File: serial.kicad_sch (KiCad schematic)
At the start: 61 parts, among them J201 Debug, J202 RS-232, J203 RS-485/422, U201 ADM213, U202 SP330

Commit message: Revisit 3D models
Signed-off-by: Benedikt Spranger <b.spranger@linutronix.de>
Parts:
- D201, D202, D203, D204, D205, D206, D207, D208, D209, D210, D211, D212, D213, D214: footprint LED_SMD:LED_Kingbright_AAA3528ESGCT -> fixes:LED_Kingbright_AAA3528ESGCT
- J203: footprint TerminalBlock_WAGO:TerminalBlock_WAGO_236-404_1x04_P5.00mm_45Degree -> fixes:TerminalBlock_WAGO_236-404_1x04_P5.00mm_45Degree
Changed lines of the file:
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@@
 			)
 		)
-		(property "Footprint" "LED_SMD:LED_Kingbright_AAA3528ESGCT"
+		(property "Footprint" "fixes:LED_Kingbright_AAA3528ESGCT"
 			(at 241.3 148.082 0)
 			(effects
@@
 			)
 		)
-		(property "Footprint" "LED_SMD:LED_Kingbright_AAA3528ESGCT"
+		(property "Footprint" "fixes:LED_Kingbright_AAA3528ESGCT"
 			(at 215.9 148.082 0)
 			(effects
@@
 			)
 		)
-		(property "Footprint" "LED_SMD:LED_Kingbright_AAA3528ESGCT"
+		(property "Footprint" "fixes:LED_Kingbright_AAA3528ESGCT"
 			(at 215.9 97.282 0)
 			(effects
@@
 			)
 		)
-		(property "Footprint" "LED_SMD:LED_Kingbright_AAA3528ESGCT"
+		(property "Footprint" "fixes:LED_Kingbright_AAA3528ESGCT"
 			(at 62.23 46.482 0)
 			(effects
@@
 			)
 		)
-		(property "Footprint" "LED_SMD:LED_Kingbright_AAA3528ESGCT"
+		(property "Footprint" "fixes:LED_Kingbright_AAA3528ESGCT"
 			(at 114.3 46.482 0)
 			(effects
@@
 			)
 		)
-		(property "Footprint" "LED_SMD:LED_Kingbright_AAA3528ESGCT"
+		(property "Footprint" "fixes:LED_Kingbright_AAA3528ESGCT"
 			(at 241.3 97.282 0)
 			(effects
@@
 			)
 		)
-		(property "Footprint" "LED_SMD:LED_Kingbright_AAA3528ESGCT"
+		(property "Footprint" "fixes:LED_Kingbright_AAA3528ESGCT"
 			(at 215.9 46.482 0)
 			(effects
@@
 			)
 		)
-		(property "Footprint" "LED_SMD:LED_Kingbright_AAA3528ESGCT"
+		(property "Footprint" "fixes:LED_Kingbright_AAA3528ESGCT"
 			(at 139.7 46.482 0)
 			(effects
@@
 			)
 		)
-		(property "Footprint" "LED_SMD:LED_Kingbright_AAA3528ESGCT"
+		(property "Footprint" "fixes:LED_Kingbright_AAA3528ESGCT"
 			(at 165.1 46.482 0)
 			(effects
@@
 			)
 		)
-		(property "Footprint" "LED_SMD:LED_Kingbright_AAA3528ESGCT"
+		(property "Footprint" "fixes:LED_Kingbright_AAA3528ESGCT"
 			(at 36.83 46.482 0)
 			(effects
@@
 			)
 		)
-		(property "Footprint" "LED_SMD:LED_Kingbright_AAA3528ESGCT"
+		(property "Footprint" "fixes:LED_Kingbright_AAA3528ESGCT"
 			(at 88.9 46.482 0)
 			(effects
@@
 			)
 		)
-		(property "Footprint" "LED_SMD:LED_Kingbright_AAA3528ESGCT"
+		(property "Footprint" "fixes:LED_Kingbright_AAA3528ESGCT"
 			(at 241.3 46.482 0)
 			(effects
@@
 			)
 		)
-		(property "Footprint" "LED_SMD:LED_Kingbright_AAA3528ESGCT"
+		(property "Footprint" "fixes:LED_Kingbright_AAA3528ESGCT"
 			(at 190.5 46.482 0)
 			(effects
@@
 			)
 		)
-		(property "Footprint" "LED_SMD:LED_Kingbright_AAA3528ESGCT"
+		(property "Footprint" "fixes:LED_Kingbright_AAA3528ESGCT"
 			(at 266.7 46.482 0)
 			(effects
@@
 			)
 		)
-		(property "Footprint" "TerminalBlock_WAGO:TerminalBlock_WAGO_236-404_1x04_P5.00mm_45Degree"
+		(property "Footprint" "fixes:TerminalBlock_WAGO_236-404_1x04_P5.00mm_45Degree"
 			(at 187.96 137.16 0)
 			(effects

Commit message: Fix Dual LED footprint issue
Signed-off-by: Benedikt Spranger <b.spranger@linutronix.de>
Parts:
- D201, D202, D203, D204, D205, D206, D207, D208, D209, D210, D211, D212, D213, D214: symbol Device:LED_Dual_AAKK -> led:LED_Dual_KAAK
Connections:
- net CTS: now also D212.1 (K2); no longer D212.4 (K2)
- net GND: now also D201.4 (K1), D202.4 (K1), D203.4 (K1), D204.4 (K1), D205.4 (K1), D206.4 (K1), D207.4 (K1), D208.4 (K1), D209.4 (K1), D210.4 (K1), D211.4 (K1), D212.4 (K1), D213.4 (K1), D214.4 (K1); no longer D201.3 (K1), D202.3 (K1), D203.3 (K1), D204.3 (K1), D205.3 (K1), D206.3 (K1), D207.3 (K1), D208.3 (K1), D209.3 (K1), D210.3 (K1), D211.3 (K1), D212.3 (K1), D213.3 (K1), D214.3 (K1)
- net RTS: now also D213.1 (K2); no longer D213.4 (K2)
- net RXD: now also D210.1 (K2); no longer D210.4 (K2)
- net TXD: now also D209.1 (K2); no longer D209.4 (K2)
- net USART2_CTS: now also D205.1 (K2); no longer D205.4 (K2)
- net USART2_DCD: now also D207.1 (K2); no longer D207.4 (K2)
- net USART2_DSR: now also D208.1 (K2); no longer D208.4 (K2)
- net USART2_DTR: now also D211.1 (K2); no longer D211.4 (K2)
- net USART2_RI: now also D214.1 (K2); no longer D214.4 (K2)
- net USART2_RTS: now also D206.1 (K2); no longer D206.4 (K2)
- net USART2_RX: now also D203.1 (K2); no longer D203.4 (K2)
- net USART2_TX: now also D204.1 (K2); no longer D204.4 (K2)
- net USART3_RX: now also D201.1 (K2); no longer D201.4 (K2)
- net USART3_TX: now also D202.1 (K2); no longer D202.4 (K2)
- net at R230.2: now also D213.3 (A1); no longer D213.1 (A1)
- net at R224.2: now also D210.3 (A1); no longer D210.1 (A1)
- net at R223.2: now also D209.3 (A1); no longer D209.1 (A1)
- net at R229.2: now also D212.3 (A1); no longer D212.1 (A1)
- net at R212.2: now also D206.3 (A1); no longer D206.1 (A1)
- net at R204.2: now also D202.3 (A1); no longer D202.1 (A1)
- net at R208.2: now also D204.3 (A1); no longer D204.1 (A1)
- net at R222.2: now also D208.3 (A1); no longer D208.1 (A1)
- net at R210.2: now also D205.3 (A1); no longer D205.1 (A1)
- net at R202.2: now also D201.3 (A1); no longer D201.1 (A1)
- net at R206.2: now also D203.3 (A1); no longer D203.1 (A1)
- net at R218.2: now also D207.3 (A1); no longer D207.1 (A1)
- net at R228.2: now also D211.3 (A1); no longer D211.1 (A1)
- net at R232.2: now also D214.3 (A1); no longer D214.1 (A1)
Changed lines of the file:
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@@
 	)
 	(symbol
-		(lib_id "Device:LED_Dual_AAKK")
+		(lib_id "led:LED_Dual_KAAK")
 		(at 241.3 147.32 270)
 		(unit 1)
@@
 			)
 		)
-		(property "Description" "Dual LED, cathodes on pins 3 and 4"
+		(property "Description" "Dual LED, cathodes on pins 1 and 4"
 			(at 241.3 147.32 0)
 			(effects
@@
 	)
 	(symbol
-		(lib_id "Device:LED_Dual_AAKK")
+		(lib_id "led:LED_Dual_KAAK")
 		(at 215.9 147.32 270)
 		(unit 1)
@@
 			)
 		)
-		(property "Description" "Dual LED, cathodes on pins 3 and 4"
+		(property "Description" "Dual LED, cathodes on pins 1 and 4"
 			(at 215.9 147.32 0)
 			(effects
@@
 	)
 	(symbol
-		(lib_id "Device:LED_Dual_AAKK")
+		(lib_id "led:LED_Dual_KAAK")
 		(at 215.9 96.52 270)
 		(unit 1)
@@
 			)
 		)
-		(property "Description" "Dual LED, cathodes on pins 3 and 4"
+		(property "Description" "Dual LED, cathodes on pins 1 and 4"
 			(at 215.9 96.52 0)
 			(effects
@@
 	)
 	(symbol
-		(lib_id "Device:LED_Dual_AAKK")
+		(lib_id "led:LED_Dual_KAAK")
 		(at 62.23 45.72 270)
 		(unit 1)
@@
 			)
 		)
-		(property "Description" "Dual LED, cathodes on pins 3 and 4"
+		(property "Description" "Dual LED, cathodes on pins 1 and 4"
 			(at 62.23 45.72 0)
 			(effects
@@
 	)
 	(symbol
-		(lib_id "Device:LED_Dual_AAKK")
+		(lib_id "led:LED_Dual_KAAK")
 		(at 114.3 45.72 270)
 		(unit 1)
@@
 			)
 		)
-		(property "Description" "Dual LED, cathodes on pins 3 and 4"
+		(property "Description" "Dual LED, cathodes on pins 1 and 4"
 			(at 114.3 45.72 0)
 			(effects
@@
 	)
 	(symbol
-		(lib_id "Device:LED_Dual_AAKK")
+		(lib_id "led:LED_Dual_KAAK")
 		(at 241.3 96.52 270)
 		(unit 1)
@@
 			)
 		)
-		(property "Description" "Dual LED, cathodes on pins 3 and 4"
+		(property "Description" "Dual LED, cathodes on pins 1 and 4"
 			(at 241.3 96.52 0)
 			(effects
@@
 	)
 	(symbol
-		(lib_id "Device:LED_Dual_AAKK")
+		(lib_id "led:LED_Dual_KAAK")
 		(at 215.9 45.72 270)
 		(unit 1)
@@
 			)
 		)
-		(property "Description" "Dual LED, cathodes on pins 3 and 4"
+		(property "Description" "Dual LED, cathodes on pins 1 and 4"
 			(at 215.9 45.72 0)
 			(effects
@@
 	)
 	(symbol
-		(lib_id "Device:LED_Dual_AAKK")
+		(lib_id "led:LED_Dual_KAAK")
 		(at 139.7 45.72 270)
 		(unit 1)
@@
 			)
 		)
-		(property "Description" "Dual LED, cathodes on pins 3 and 4"
+		(property "Description" "Dual LED, cathodes on pins 1 and 4"
 			(at 139.7 45.72 0)
 			(effects
@@
 	)
 	(symbol
-		(lib_id "Device:LED_Dual_AAKK")
+		(lib_id "led:LED_Dual_KAAK")
 		(at 165.1 45.72 270)
 		(unit 1)
@@
 			)
 		)
-		(property "Description" "Dual LED, cathodes on pins 3 and 4"
+		(property "Description" "Dual LED, cathodes on pins 1 and 4"
 			(at 165.1 45.72 0)
 			(effects
@@
 	)
 	(symbol
-		(lib_id "Device:LED_Dual_AAKK")
+		(lib_id "led:LED_Dual_KAAK")
 		(at 36.83 45.72 270)
 		(unit 1)
@@
 			)
 		)
-		(property "Description" "Dual LED, cathodes on pins 3 and 4"
+		(property "Description" "Dual LED, cathodes on pins 1 and 4"
 			(at 36.83 45.72 0)
 			(effects
@@
 			)
 		)
+		(property "digikey#" ""
+			(at 36.83 45.72 0)
+			(effects
+				(font
+					(size 1.27 1.27)
+				)
+				(hide yes)
+			)
+		)
+		(property "tme#" ""
+			(at 36.83 45.72 0)
+			(effects
+				(font
+					(size 1.27 1.27)
+				)
+				(hide yes)
+			)
+		)
 		(pin "2"
 		)
@@
 	)
 	(symbol
-		(lib_id "Device:LED_Dual_AAKK")
+		(lib_id "led:LED_Dual_KAAK")
 		(at 88.9 45.72 270)
 		(unit 1)
@@
 			)
 		)
-		(property "Description" "Dual LED, cathodes on pins 3 and 4"
+		(property "Description" "Dual LED, cathodes on pins 1 and 4"
 			(at 88.9 45.72 0)
 			(effects
@@
 	)
 	(symbol
-		(lib_id "Device:LED_Dual_AAKK")
+		(lib_id "led:LED_Dual_KAAK")
 		(at 241.3 45.72 270)
 		(unit 1)
@@
 			)
 		)
-		(property "Description" "Dual LED, cathodes on pins 3 and 4"
+		(property "Description" "Dual LED, cathodes on pins 1 and 4"
 			(at 241.3 45.72 0)
 			(effects
@@
 	)
 	(symbol
-		(lib_id "Device:LED_Dual_AAKK")
+		(lib_id "led:LED_Dual_KAAK")
 		(at 190.5 45.72 270)
 		(unit 1)
@@
 			)
 		)
-		(property "Description" "Dual LED, cathodes on pins 3 and 4"
+		(property "Description" "Dual LED, cathodes on pins 1 and 4"
 			(at 190.5 45.72 0)
 			(effects
@@
 	)
 	(symbol
-		(lib_id "Device:LED_Dual_AAKK")
+		(lib_id "led:LED_Dual_KAAK")
 		(at 266.7 45.72 270)
 		(unit 1)
@@
 			)
 		)
-		(property "Description" "Dual LED, cathodes on pins 3 and 4"
+		(property "Description" "Dual LED, cathodes on pins 1 and 4"
 			(at 266.7 45.72 0)
 			(effects

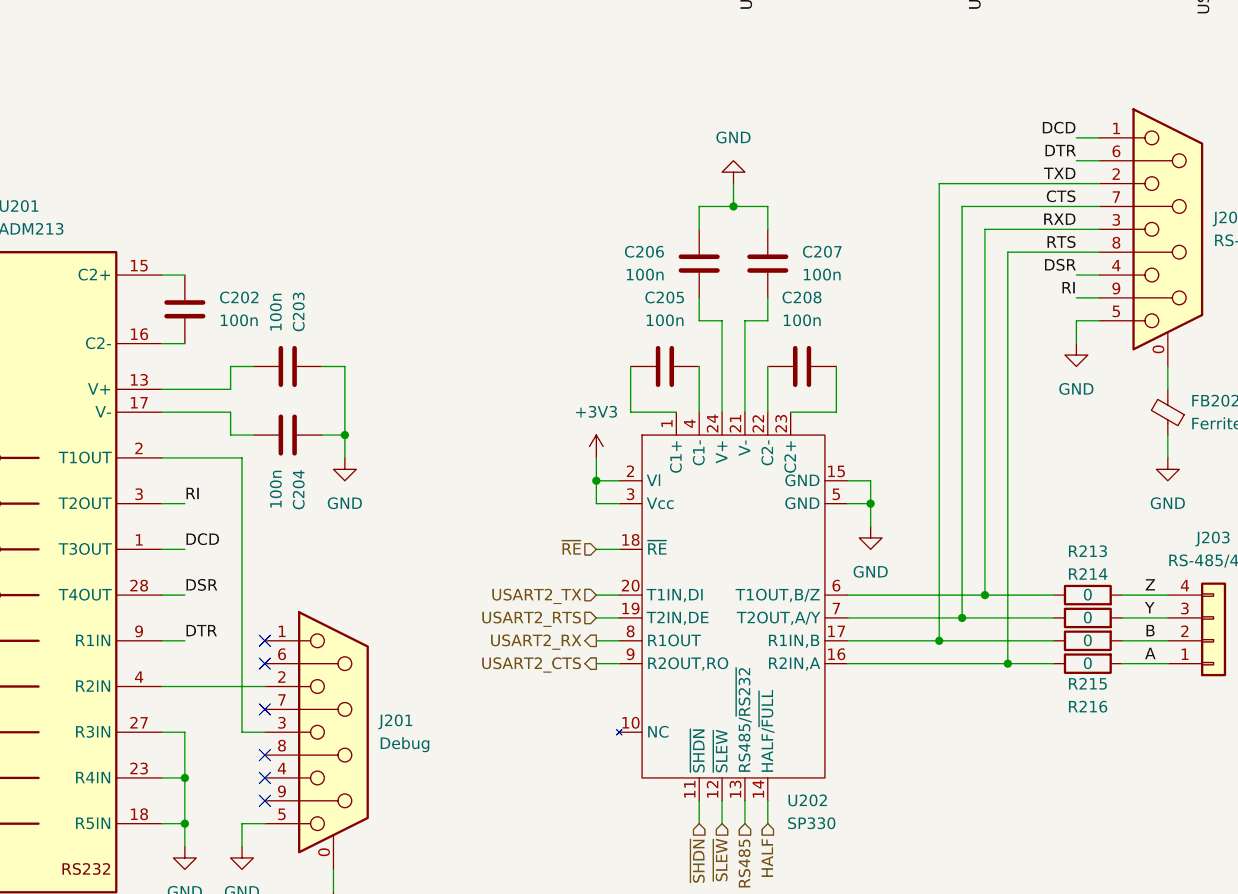
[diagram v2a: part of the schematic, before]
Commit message: Rework serial from DTE to DCE
Signed-off-by: Benedikt Spranger <b.spranger@linutronix.de>
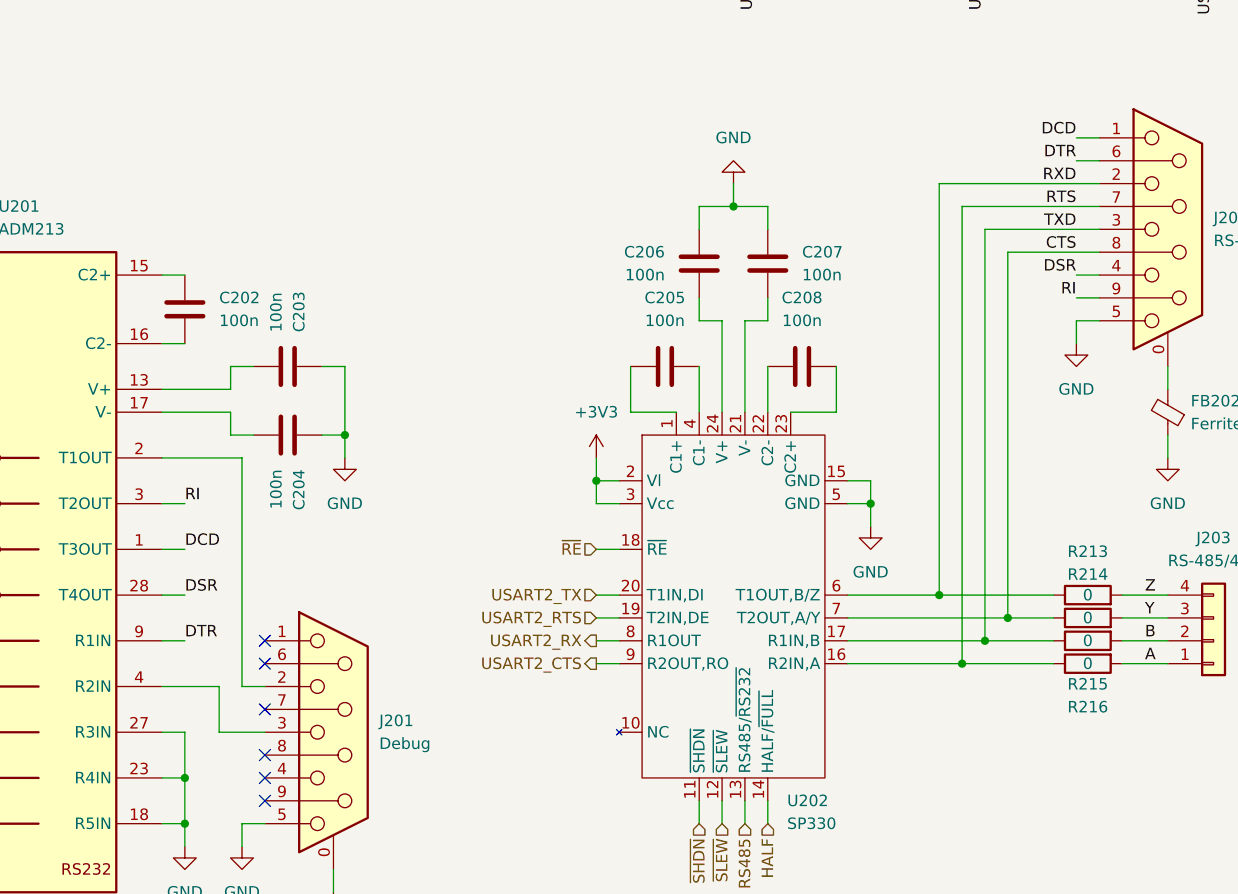
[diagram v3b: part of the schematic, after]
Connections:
- net CTS: now also J202.8; no longer J202.7
- net RTS: now also J202.7; no longer J202.8
- net RXD: now also J202.2; no longer J202.3
- net TXD: now also J202.3; no longer J202.2
- net at U201.2 (T1OUT): now also J201.2; no longer J201.3
- net at U201.4 (R2IN): now also J201.3; no longer J201.2
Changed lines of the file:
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@@
-	)
-	(junction
-		(at 165.1 139.7)
-		(diameter 0)
-		(color 0 0 0 0)
 	)
 	(junction
@@
 	)
 	(junction
+		(at 160.02 139.7)
+		(diameter 0)
+		(color 0 0 0 0)
+	)
+	(junction
+		(at 162.56 137.16)
+		(diameter 0)
+		(color 0 0 0 0)
+	)
+	(junction
+		(at 157.48 132.08)
+		(diameter 0)
+		(color 0 0 0 0)
+	)
+	(junction
 		(at 134.62 88.9)
 		(diameter 0)
@@
 	)
 	(junction
-		(at 160.02 134.62)
-		(diameter 0)
-		(color 0 0 0 0)
-	)
-	(junction
-		(at 162.56 132.08)
+		(at 165.1 134.62)
 		(diameter 0)
 		(color 0 0 0 0)
@@
 		(color 0 0 0 0)
 	)
-	(junction
-		(at 157.48 137.16)
-		(diameter 0)
-		(color 0 0 0 0)
-	)
 	(no_connect
 		(at 82.55 149.86)
@@
 	(wire
 		(pts
+			(xy 77.47 142.24) (xy 77.47 147.32)
+		)
+		(stroke
+			(width 0)
+			(type default)
+		)
+	)
+	(wire
+		(pts
 			(xy 27.94 127) (xy 30.48 127)
 		)
@@
 	(wire
 		(pts
-			(xy 165.1 93.98) (xy 165.1 139.7)
-		)
-		(stroke
-			(width 0)
-			(type default)
-		)
-	)
-	(wire
-		(pts
 			(xy 243.84 25.4) (xy 243.84 27.94)
 		)
@@
 	(wire
 		(pts
+			(xy 157.48 132.08) (xy 170.18 132.08)
+		)
+		(stroke
+			(width 0)
+			(type default)
+		)
+	)
+	(wire
+		(pts
 			(xy 243.84 53.34) (xy 243.84 55.88)
 		)
@@
 	(wire
 		(pts
-			(xy 147.32 139.7) (xy 165.1 139.7)
+			(xy 147.32 139.7) (xy 160.02 139.7)
 		)
 		(stroke
@@
 	(wire
 		(pts
-			(xy 147.32 132.08) (xy 162.56 132.08)
+			(xy 147.32 132.08) (xy 157.48 132.08)
 		)
 		(stroke
@@
 	(wire
 		(pts
-			(xy 160.02 134.62) (xy 170.18 134.62)
-		)
-		(stroke
-			(width 0)
-			(type default)
-		)
-	)
-	(wire
-		(pts
 			(xy 39.37 25.4) (xy 39.37 27.94)
 		)
@@
 	(wire
 		(pts
+			(xy 165.1 93.98) (xy 165.1 134.62)
+		)
+		(stroke
+			(width 0)
+			(type default)
+		)
+	)
+	(wire
+		(pts
 			(xy 162.56 91.44) (xy 175.26 91.44)
 		)
@@
 	(wire
 		(pts
+			(xy 165.1 134.62) (xy 170.18 134.62)
+		)
+		(stroke
+			(width 0)
+			(type default)
+		)
+	)
+	(wire
+		(pts
+			(xy 160.02 88.9) (xy 160.02 139.7)
+		)
+		(stroke
+			(width 0)
+			(type default)
+		)
+	)
+	(wire
+		(pts
 			(xy 243.84 86.36) (xy 243.84 88.9)
 		)
@@
 	(wire
 		(pts
-			(xy 160.02 88.9) (xy 160.02 134.62)
-		)
-		(stroke
-			(width 0)
-			(type default)
-		)
-	)
-	(wire
-		(pts
 			(xy 71.12 111.76) (xy 78.74 111.76)
 		)
@@
 	(wire
 		(pts
-			(xy 157.48 137.16) (xy 157.48 86.36)
-		)
-		(stroke
-			(width 0)
-			(type default)
-		)
-	)
-	(wire
-		(pts
 			(xy 218.44 53.34) (xy 218.44 55.88)
 		)
@@
 	(wire
 		(pts
-			(xy 80.01 147.32) (xy 80.01 116.84)
-		)
-		(stroke
-			(width 0)
-			(type default)
-		)
-	)
-	(wire
-		(pts
-			(xy 71.12 142.24) (xy 82.55 142.24)
-		)
-		(stroke
-			(width 0)
-			(type default)
-		)
-	)
-	(wire
-		(pts
 			(xy 172.72 96.52) (xy 175.26 96.52)
 		)
@@
 	(wire
 		(pts
-			(xy 157.48 137.16) (xy 170.18 137.16)
-		)
-		(stroke
-			(width 0)
-			(type default)
-		)
-	)
-	(wire
-		(pts
 			(xy 167.64 25.4) (xy 167.64 27.94)
 		)
@@
 	(wire
 		(pts
-			(xy 147.32 137.16) (xy 157.48 137.16)
+			(xy 147.32 137.16) (xy 162.56 137.16)
 		)
 		(stroke
@@
 	(wire
 		(pts
+			(xy 162.56 91.44) (xy 162.56 137.16)
+		)
+		(stroke
+			(width 0)
+			(type default)
+		)
+	)
+	(wire
+		(pts
 			(xy 91.44 116.84) (xy 91.44 114.3)
 		)
@@
 	(wire
 		(pts
+			(xy 157.48 86.36) (xy 157.48 132.08)
+		)
+		(stroke
+			(width 0)
+			(type default)
+		)
+	)
+	(wire
+		(pts
 			(xy 27.94 104.14) (xy 30.48 104.14)
 		)
@@
 	(wire
 		(pts
+			(xy 160.02 139.7) (xy 170.18 139.7)
+		)
+		(stroke
+			(width 0)
+			(type default)
+		)
+	)
+	(wire
+		(pts
 			(xy 165.1 93.98) (xy 175.26 93.98)
 		)
@@
 	(wire
 		(pts
+			(xy 71.12 142.24) (xy 77.47 142.24)
+		)
+		(stroke
+			(width 0)
+			(type default)
+		)
+	)
+	(wire
+		(pts
 			(xy 238.76 35.56) (xy 238.76 38.1)
 		)
@@
 	(wire
 		(pts
+			(xy 77.47 147.32) (xy 82.55 147.32)
+		)
+		(stroke
+			(width 0)
+			(type default)
+		)
+	)
+	(wire
+		(pts
 			(xy 213.36 35.56) (xy 213.36 38.1)
 		)
@@
 	(wire
 		(pts
-			(xy 147.32 134.62) (xy 160.02 134.62)
+			(xy 147.32 134.62) (xy 165.1 134.62)
 		)
 		(stroke
@@
 	(wire
 		(pts
+			(xy 80.01 142.24) (xy 80.01 116.84)
+		)
+		(stroke
+			(width 0)
+			(type default)
+		)
+	)
+	(wire
+		(pts
 			(xy 39.37 53.34) (xy 39.37 55.88)
 		)
@@
 	(wire
 		(pts
-			(xy 165.1 139.7) (xy 170.18 139.7)
-		)
-		(stroke
-			(width 0)
-			(type default)
-		)
-	)
-	(wire
-		(pts
 			(xy 149.86 121.92) (xy 149.86 124.46)
 		)
@@
 	(wire
 		(pts
-			(xy 162.56 132.08) (xy 170.18 132.08)
-		)
-		(stroke
-			(width 0)
-			(type default)
-		)
-	)
-	(wire
-		(pts
-			(xy 162.56 91.44) (xy 162.56 132.08)
+			(xy 80.01 142.24) (xy 82.55 142.24)
 		)
 		(stroke
@@
 	(wire
 		(pts
-			(xy 82.55 147.32) (xy 80.01 147.32)
-		)
-		(stroke
-			(width 0)
-			(type default)
-		)
-	)
-	(wire
-		(pts
 			(xy 177.8 137.16) (xy 182.88 137.16)
+		)
+		(stroke
+			(width 0)
+			(type default)
+		)
+	)
+	(wire
+		(pts
+			(xy 162.56 137.16) (xy 170.18 137.16)
 		)
 		(stroke
@@
 	)
 	(label "TXD"
-		(at 172.72 86.36 180)
+		(at 172.72 91.44 180)
 		(effects
 			(font
@@
 	)
 	(label "CTS"
-		(at 172.72 88.9 180)
+		(at 172.72 93.98 180)
 		(effects
 			(font
@@
 	)
 	(label "RXD"
-		(at 172.72 91.44 180)
+		(at 172.72 86.36 180)
 		(effects
 			(font
@@
 	)
 	(label "RTS"
-		(at 172.72 93.98 180)
-		(effects
-			(font
+		(at 172.72 88.9 180)
+		(effects
+			(font
